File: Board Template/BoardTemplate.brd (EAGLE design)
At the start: 101.6 x 101.6 mm, 1 part

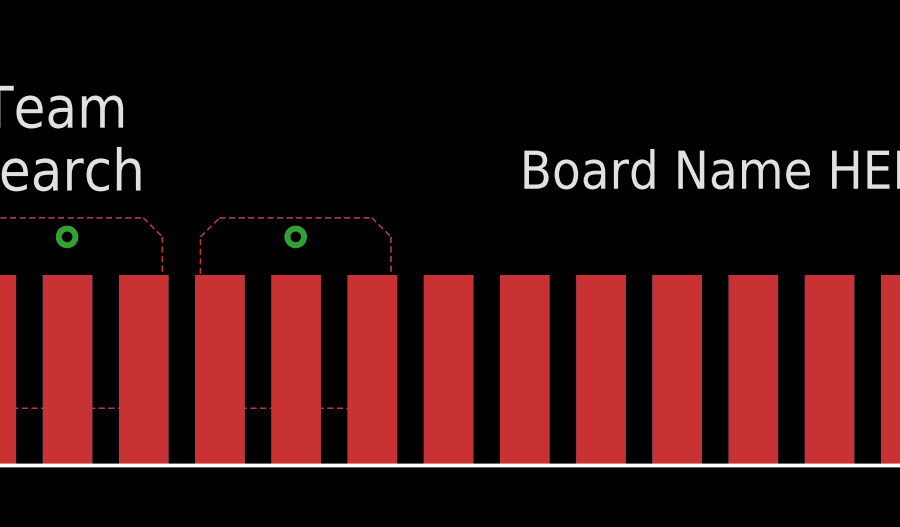
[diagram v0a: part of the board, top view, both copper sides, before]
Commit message: New schematic template and converter fixes
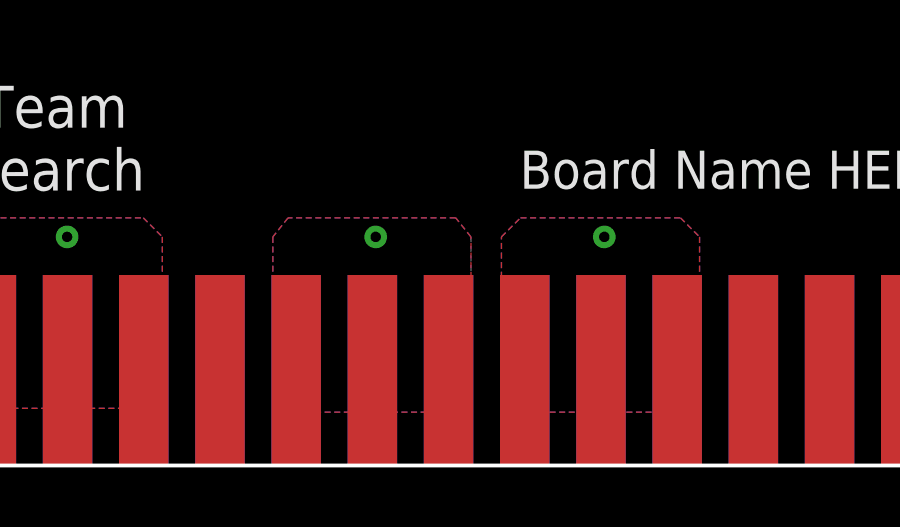
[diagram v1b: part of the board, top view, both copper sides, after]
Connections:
- new net +3V3: U$1.1, U$1.2, U$1.3, U$1.54, U$1.55, U$1.56
- new net +5V: U$1.11, U$1.12, U$1.13, U$1.44, U$1.45, U$1.46
- new net GND: U$1.10, U$1.4, U$1.47, U$1.48, U$1.49, U$1.5, U$1.51, U$1.52, U$1.53, U$1.6, U$1.8, U$1.9
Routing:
- added copper zone on layer 1, net +3V3
- added copper zone on layer 16, net +3V3
- added copper zone on layer 1, net +5V
- added copper zone on layer 16, net +5V
- removed copper zone on layer 1, net 3.3V
- removed copper zone on layer 16, net 3.3V
- removed copper zone on layer 1, net 5V
- removed copper zone on layer 16, net 5V

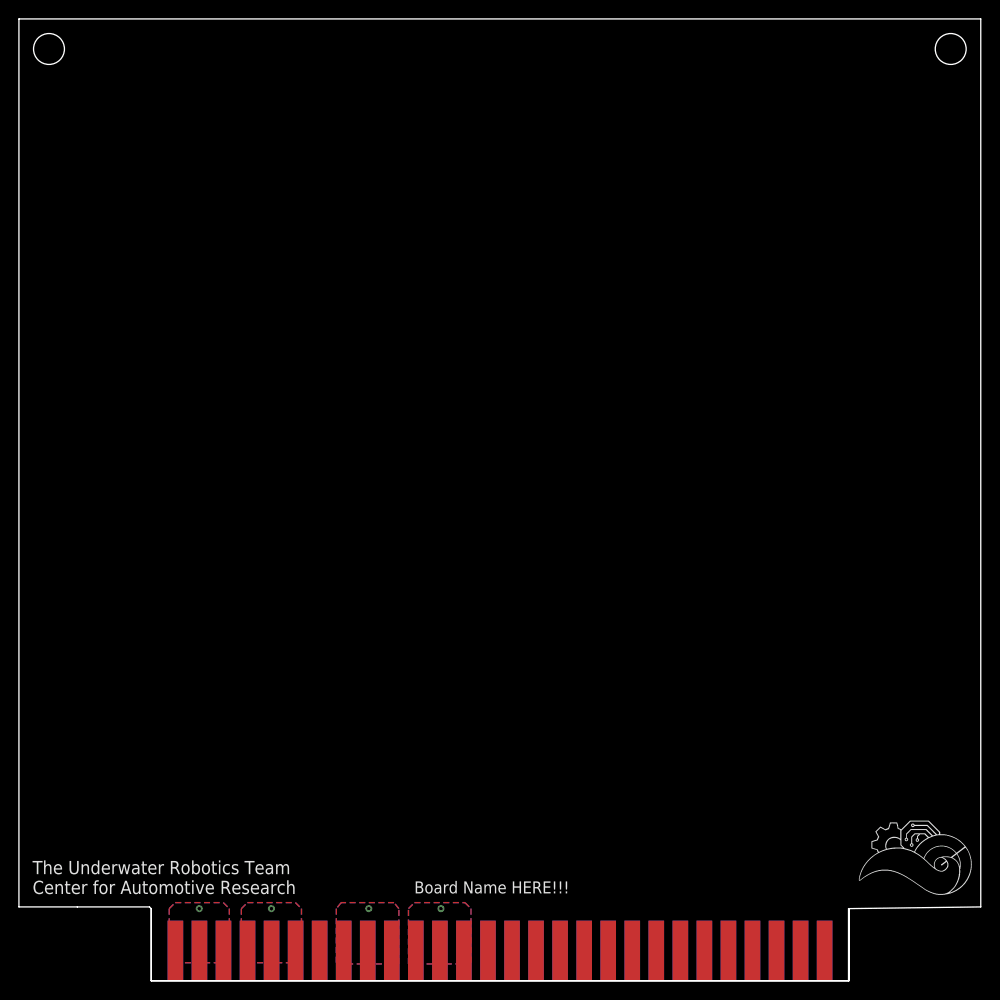
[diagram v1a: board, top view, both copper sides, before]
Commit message: Removing errors from board template
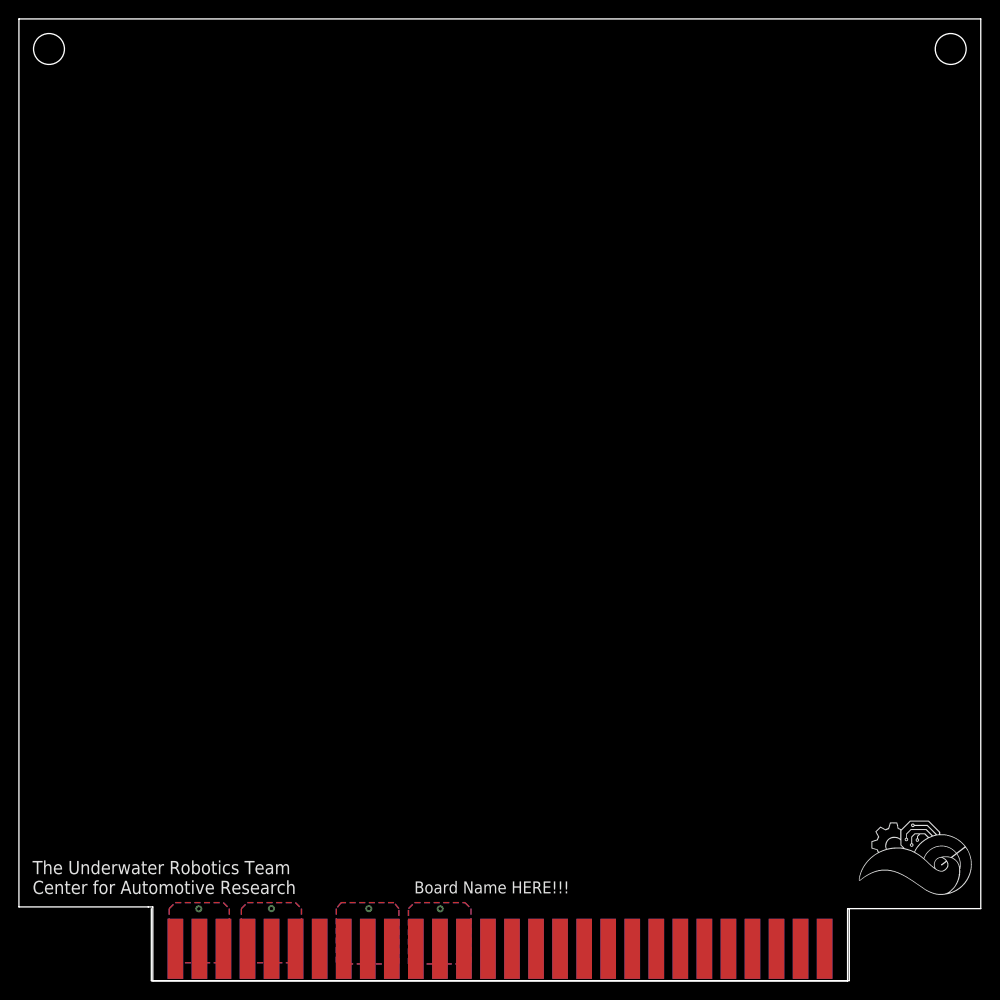
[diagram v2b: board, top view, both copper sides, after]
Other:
- outline, holes or cut-outs redrawn
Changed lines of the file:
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@@
 <setting verticaltext="up"/>
 </settings>
-<grid distance="0.005" unitdist="inch" unit="inch" style="lines" multiple="1" display="yes" altdistance="5" altunitdist="mil" altunit="mil"/>
+<grid distance="0.1" unitdist="mm" unit="mm" style="lines" multiple="1" display="yes" altdistance="5" altunitdist="mil" altunit="mil"/>
 <layers>
 <layer number="1" name="Top" color="4" fill="1" visible="yes" active="yes"/>
@@
 <board>
 <plain>
-<wire x1="0" y1="7.8" x2="6.17" y2="7.8" width="0" layer="20"/>
-<wire x1="6.17" y1="7.8" x2="13.79" y2="7.8" width="0" layer="20"/>
-<wire x1="13.79" y1="7.8" x2="13.97" y2="7.62" width="0" layer="20"/>
-<wire x1="13.97" y1="7.62" x2="13.97" y2="0" width="0" layer="20"/>
-<wire x1="13.97" y1="0" x2="87.63" y2="0" width="0" layer="20"/>
-<wire x1="87.63" y1="0" x2="87.63" y2="7.62" width="0" layer="20"/>
-<wire x1="87.63" y1="7.62" x2="101.6" y2="7.8" width="0" layer="20"/>
-<wire x1="101.6" y1="7.8" x2="101.6" y2="101.6" width="0" layer="20"/>
+<wire x1="0" y1="7.8" x2="13.663" y2="7.8" width="0" layer="20"/>
+<wire x1="13.663" y1="7.8" x2="14.143" y2="7.8" width="0" layer="20"/>
+<wire x1="14.143" y1="7.8" x2="14.143" y2="0" width="0" layer="20"/>
+<wire x1="14.143" y1="0" x2="87.53" y2="0" width="0" layer="20"/>
+<wire x1="87.53" y1="0" x2="87.53" y2="7.62" width="0" layer="20"/>
+<wire x1="87.53" y1="7.62" x2="101.6" y2="7.62" width="0" layer="20"/>
+<wire x1="101.6" y1="7.62" x2="101.6" y2="101.6" width="0" layer="20"/>
 <wire x1="101.6" y1="101.6" x2="0" y2="101.6" width="0" layer="20"/>
 <wire x1="0" y1="101.6" x2="0" y2="7.8" width="0" layer="20"/>
@@
 </class>
 </classes>
-<designrules name="default">
+<designrules name="default *">
 <description language="de">&lt;b&gt;EAGLE Design Rules&lt;/b&gt;
 &lt;p&gt;
@@
 <param name="mdViaViaSameLayer" value="6mil"/>
 <param name="mnLayersViaInSmd" value="2"/>
-<param name="mdCopperDimension" value="40mil"/>
+<param name="mdCopperDimension" value="0.00508125mm"/>
 <param name="mdDrill" value="6mil"/>
 <param name="mdSmdStop" value="0mil"/>
@@
 <vertex x="47.752" y="1.778"/>
 </polygon>
-<via x="44.577" y="7.62" extent="1-16" drill="0.35"/>
+<via x="44.5" y="7.6" extent="1-16" drill="0.35"/>
 </signal>
 <signal name="+3V3">
@@
 <vertex x="15.875" y="1.905"/>
 </polygon>
-<via x="19.05" y="7.62" extent="1-16" drill="0.35"/>
+<via x="19" y="7.6" extent="1-16" drill="0.35"/>
 </signal>
 </signals>
